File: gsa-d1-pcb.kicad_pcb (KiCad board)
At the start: 2 copper layers, 100 x 100 mm, 0 parts

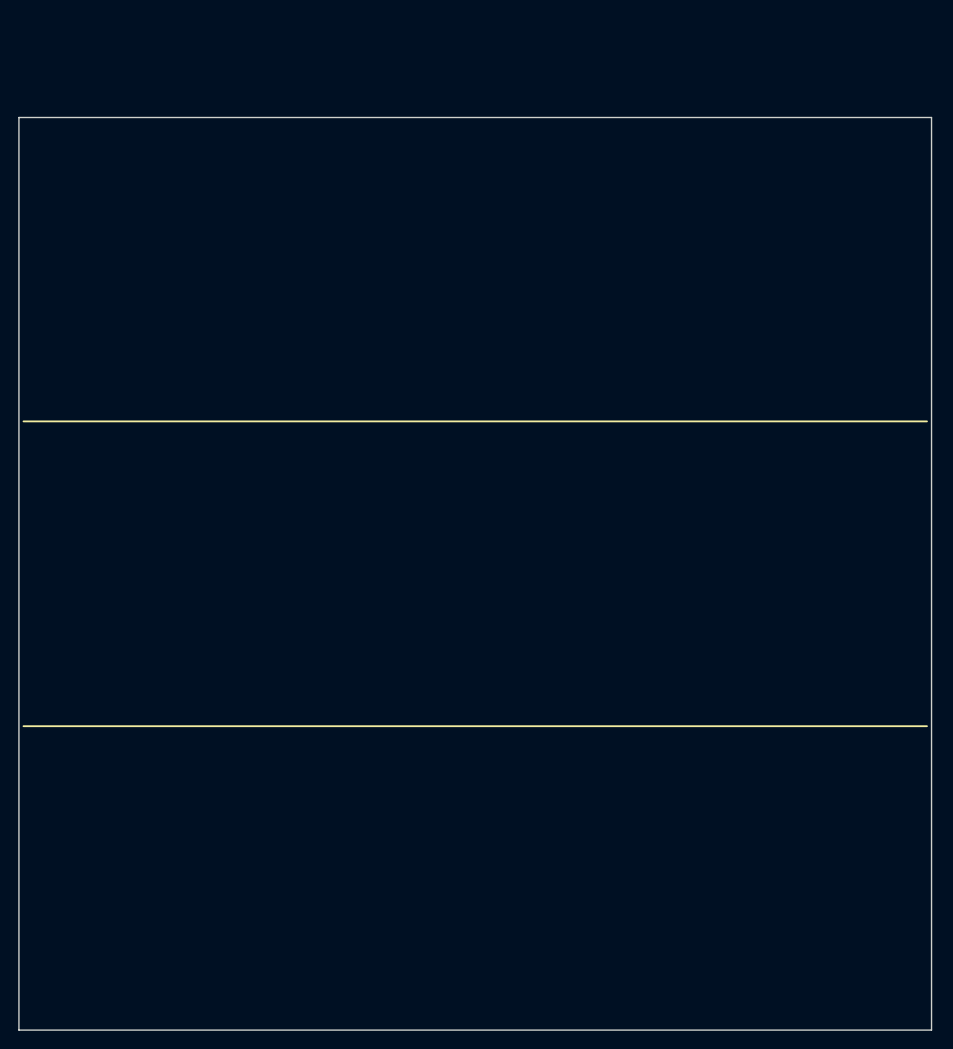
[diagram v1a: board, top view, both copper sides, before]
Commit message: Updated to use gsa-lib v1.1
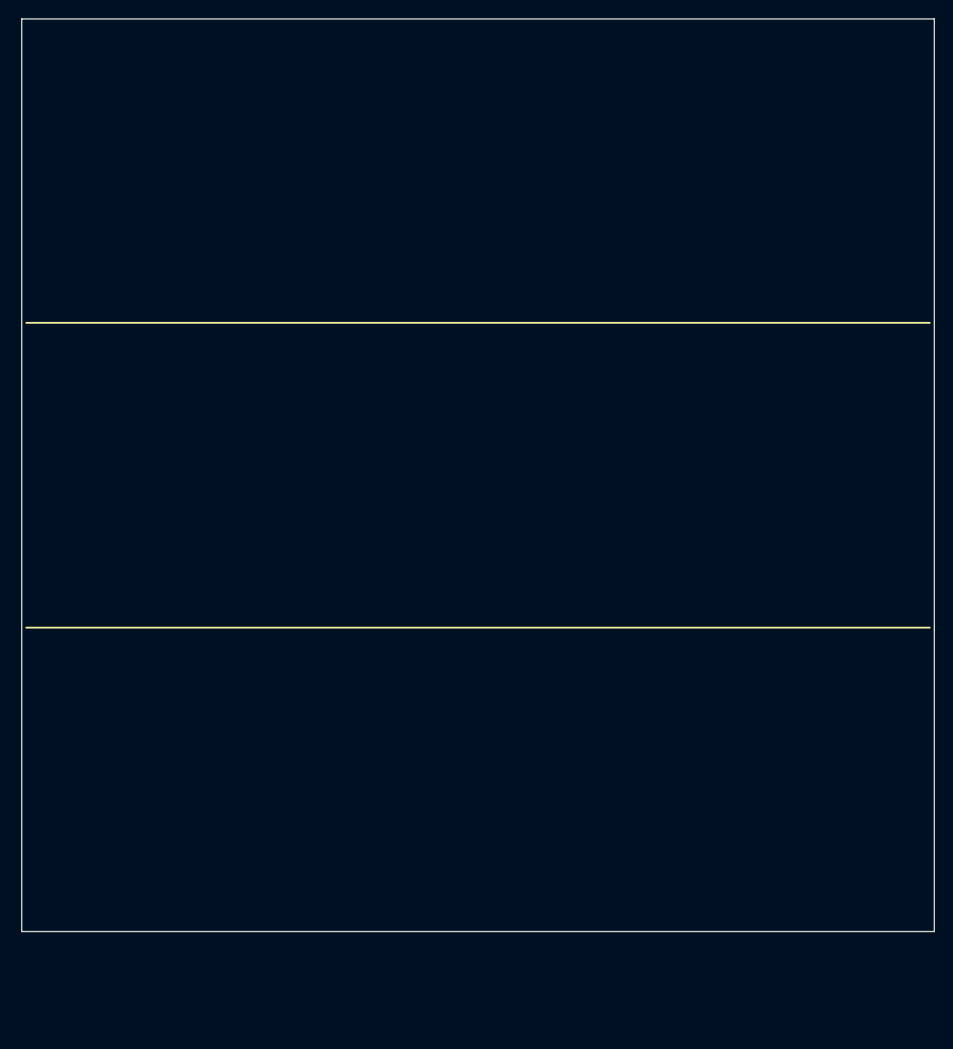
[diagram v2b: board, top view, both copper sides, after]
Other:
- net class Default: clearance 0.254 -> 0.2; trace_width 0.762 -> 0.25; via_dia 1.524 -> 0.8; via_drill 0.7 -> 0.4
- rule pad_to_mask_clearance: 0.2 -> 0.05
- rule trace_clearance: 0.254 -> 0.2
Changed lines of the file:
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@@
-(kicad_pcb (version 20171130) (host pcbnew 5.1.2-f72e74a~84~ubuntu18.04.1)
+(kicad_pcb (version 20171130) (host pcbnew 5.1.6-c6e7f7d~86~ubuntu18.04.1)
   (general
     (thickness 1.6)
@@
   (title_block
     (title Diamond-1)
-    (date "May 2019")
-    (rev 2.0.0)
+    (date "May 2020")
+    (rev 2.0.1)
     (company "Gemstone Amplication")
-    (comment 1 "© Tim Baldwin 2016,2019")
+    (comment 1 "© Tim Baldwin 2016,2020")
     (comment 2 GSA-D1)
     (comment 3 "Combined PCBs")
@@
     (0 F.Cu signal)
     (31 B.Cu signal)
-    (32 B.Adhes user)
-    (33 F.Adhes user)
-    (34 B.Paste user)
-    (35 F.Paste user)
+    (32 B.Adhes user hide)
+    (33 F.Adhes user hide)
+    (34 B.Paste user hide)
+    (35 F.Paste user hide)
     (36 B.SilkS user)
     (37 F.SilkS user)
-    (38 B.Mask user)
-    (39 F.Mask user)
+    (38 B.Mask user hide)
+    (39 F.Mask user hide)
     (40 Dwgs.User user)
-    (41 Cmts.User user)
-    (42 Eco1.User user)
-    (43 Eco2.User user)
+    (41 Cmts.User user hide)
+    (42 Eco1.User user hide)
+    (43 Eco2.User user hide)
     (44 Edge.Cuts user)
-    (45 Margin user)
-    (46 B.CrtYd user)
-    (47 F.CrtYd user)
-    (48 B.Fab user)
-    (49 F.Fab user)
+    (45 Margin user hide)
+    (46 B.CrtYd user hide)
+    (47 F.CrtYd user hide)
+    (48 B.Fab user hide)
+    (49 F.Fab user hide)
   )
   (setup
-    (last_trace_width 0.762)
-    (user_trace_width 0.254)
-    (user_trace_width 0.508)
-    (user_trace_width 0.635)
-    (user_trace_width 0.762)
-    (user_trace_width 1.27)
-    (user_trace_width 1.524)
-    (user_trace_width 2.032)
-    (user_trace_width 2.54)
-    (user_trace_width 0.254)
-    (user_trace_width 0.508)
-    (user_trace_width 0.635)
-    (user_trace_width 0.762)
-    (user_trace_width 1.27)
-    (user_trace_width 1.524)
-    (user_trace_width 2.032)
-    (user_trace_width 2.54)
-    (user_trace_width 0.254)
-    (user_trace_width 0.508)
-    (user_trace_width 0.635)
-    (user_trace_width 0.762)
-    (user_trace_width 1.27)
-    (user_trace_width 1.524)
-    (user_trace_width 2.032)
-    (user_trace_width 2.54)
-    (user_trace_width 0.254)
-    (user_trace_width 0.508)
-    (user_trace_width 0.635)
-    (user_trace_width 0.762)
-    (user_trace_width 1.27)
-    (user_trace_width 1.524)
-    (user_trace_width 2.032)
-    (user_trace_width 2.54)
-    (user_trace_width 0.254)
-    (user_trace_width 0.508)
-    (user_trace_width 0.635)
-    (user_trace_width 0.762)
-    (user_trace_width 1.27)
-    (user_trace_width 1.524)
-    (user_trace_width 2.032)
-    (user_trace_width 2.54)
-    (user_trace_width 0.254)
-    (user_trace_width 0.508)
-    (user_trace_width 0.635)
-    (user_trace_width 0.762)
-    (user_trace_width 1.27)
-    (user_trace_width 1.524)
-    (user_trace_width 2.032)
-    (user_trace_width 2.54)
-    (user_trace_width 0.254)
-    (user_trace_width 0.508)
-    (user_trace_width 0.635)
-    (user_trace_width 0.762)
-    (user_trace_width 1.27)
-    (user_trace_width 1.524)
-    (user_trace_width 2.032)
-    (user_trace_width 2.54)
-    (user_trace_width 0.254)
-    (user_trace_width 0.508)
-    (user_trace_width 0.635)
-    (user_trace_width 0.762)
-    (user_trace_width 1.27)
-    (user_trace_width 1.524)
-    (user_trace_width 2.032)
-    (user_trace_width 2.54)
-    (user_trace_width 0.254)
-    (user_trace_width 0.508)
-    (user_trace_width 0.635)
-    (user_trace_width 0.762)
-    (user_trace_width 1.27)
-    (user_trace_width 1.524)
-    (user_trace_width 2.032)
-    (user_trace_width 2.54)
-    (trace_clearance 0.254)
+    (last_trace_width 0.25)
+    (trace_clearance 0.2)
     (zone_clearance 0.508)
     (zone_45_only no)
     (trace_min 0.2)
-    (via_size 1.524)
-    (via_drill 0.7)
+    (via_size 0.8)
+    (via_drill 0.4)
     (via_min_size 0.4)
     (via_min_drill 0.3)
-    (user_via 1.27 0.7)
-    (user_via 1.524 0.7)
-    (user_via 1.27 0.7)
-    (user_via 1.524 0.7)
     (uvia_size 0.3)
     (uvia_drill 0.1)
@@
     (uvia_min_size 0.2)
     (uvia_min_drill 0.1)
-    (edge_width 0.15)
+    (edge_width 0.05)
     (segment_width 0.2)
     (pcb_text_width 0.3)
     (pcb_text_size 1.5 1.5)
-    (mod_edge_width 0.15)
+    (mod_edge_width 0.12)
     (mod_text_size 1 1)
     (mod_text_width 0.15)
-    (pad_size 1.984375 1.984375)
-    (pad_drill 1)
-    (pad_to_mask_clearance 0.2)
-    (aux_axis_origin 99.695 50.8)
-    (grid_origin 99.695 50.8)
-    (visible_elements 7FFFFF7F)
+    (pad_size 1.524 1.524)
+    (pad_drill 0.762)
+    (pad_to_mask_clearance 0.05)
+    (aux_axis_origin 0 0)
+    (visible_elements FFFFFF7F)
     (pcbplotparams
-      (layerselection 0x010f0_80000001)
-      (usegerberextensions true)
-      (usegerberattributes false)
-      (usegerberadvancedattributes false)
-      (creategerberjobfile false)
+      (layerselection 0x010fc_ffffffff)
+      (usegerberextensions false)
+      (usegerberattributes true)
+      (usegerberadvancedattributes true)
+      (creategerberjobfile true)
       (excludeedgelayer true)
       (linewidth 0.100000)
@@
       (viasonmask false)
       (mode 1)
-      (useauxorigin true)
+      (useauxorigin false)
       (hpglpennumber 1)
       (hpglpenspeed 20)
@@
       (psa4output false)
       (plotreference true)
-      (plotvalue false)
+      (plotvalue true)
       (plotinvisibletext false)
       (padsonsilk false)
-      (subtractmaskfromsilk true)
+      (subtractmaskfromsilk false)
       (outputformat 1)
       (mirror false)
-      (drillshape 0)
+      (drillshape 1)
       (scaleselection 1)
-      (outputdirectory "gerber/"))
+      (outputdirectory ""))
   )
   (net 0 "")
   (net_class Default "This is the default net class."
-    (clearance 0.254)
-    (trace_width 0.762)
-    (via_dia 1.524)
-    (via_drill 0.7)
+    (clearance 0.2)
+    (trace_width 0.25)
+    (via_dia 0.8)
+    (via_drill 0.4)
     (uvia_dia 0.3)
     (uvia_drill 0.1)
   )
-  (gr_text "Board Size: 100mm x 100mm\nDivided at 33.3mm and 66.7mm" (at 148.59 22.86) (layer Dwgs.User)
+  (gr_line (start 100.5 106.7) (end 199.5 106.7) (angle 90) (layer F.SilkS) (width 0.2))
+  (gr_line (start 100 40) (end 200 40) (angle 90) (layer Edge.Cuts) (width 0.15))
+  (gr_text "Board Size: 100mm x 100mm\nDivided at 33.3mm and 66.7mm" (at 150.8 32.38) (layer Dwgs.User)
     (effects (font (size 1.5 1.5) (thickness 0.3)))
   )
-  (gr_line (start 100.195 117.5) (end 199.195 117.5) (angle 90) (layer B.SilkS) (width 0.2))
-  (gr_line (start 100.195 117.5) (end 199.195 117.5) (angle 90) (layer F.SilkS) (width 0.2))
-  (gr_line (start 100.195 84.1) (end 199.195 84.1) (angle 90) (layer B.SilkS) (width 0.2))
-  (gr_line (start 100.195 84.1) (end 199.195 84.1) (angle 90) (layer F.SilkS) (width 0.2))
-  (gr_line (start 99.695 150.8) (end 99.695 50.8) (angle 90) (layer Edge.Cuts) (width 0.15))
-  (gr_line (start 199.695 150.8) (end 99.695 150.8) (angle 90) (layer Edge.Cuts) (width 0.15))
-  (gr_line (start 199.695 50.8) (end 199.695 150.8) (angle 90) (layer Edge.Cuts) (width 0.15))
-  (gr_line (start 99.695 50.8) (end 199.695 50.8) (angle 90) (layer Edge.Cuts) (width 0.15))
+  (gr_line (start 100.5 106.7) (end 199.5 106.7) (angle 90) (layer B.SilkS) (width 0.2))
+  (gr_line (start 100.5 73.3) (end 199.5 73.3) (angle 90) (layer B.SilkS) (width 0.2))
+  (gr_line (start 100 140) (end 100 40) (angle 90) (layer Edge.Cuts) (width 0.15))
+  (gr_line (start 100.5 73.3) (end 199.5 73.3) (angle 90) (layer F.SilkS) (width 0.2))
+  (gr_line (start 200 140) (end 100 140) (angle 90) (layer Edge.Cuts) (width 0.15))
+  (gr_line (start 200 40) (end 200 140) (angle 90) (layer Edge.Cuts) (width 0.15))
 )
